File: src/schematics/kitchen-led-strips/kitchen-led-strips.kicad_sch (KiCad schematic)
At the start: 75 parts, among them Q1 BC847BS, Q2 BC847BS, U1 DML3006LFDS, U2 AP62150WU, U3 PIC16F15355-I/MV

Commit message: Started work on the PCB.
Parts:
- CONN1: renamed from CONN1a; footprint restall-generic-connectors:th-header-1x2-2.54mm-vertical -> restall-generic-connectors:th-header-1x2-5.08mm-vertical
- CONN2: renamed from CONN2a; footprint restall-generic-connectors:th-header-1x2-2.54mm-vertical -> restall-generic-connectors:th-header-1x2-5.08mm-vertical
- renumbered CONN1 to CONN-PNL1, CONN2 to CONN-PNL2, CONN2b to CONN3, CONN3 to CONN4, CONN4 to CONN5, CONN5 to CONN6, CONN6 to CONN7
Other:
- note added: "Ensure 2.5mm^{2} hole sizes for CONN1 and CONN2."
- note added: "Pin 2 of CONN2 provides flexibility in routing ground return currents."
- note added: "Pins 2 and 3 provide flexibility in routing ground return currents for the fast LED_{Dx} edges whilst avoiding potentially large DC return. Ensure 1.5mm^{2} hole sizes."
- note removed: "Pin 2 of CONN2a provides flexibility in routing ground return currents."
- note removed: "Pins 2 and 3 provide flexibility in routing ground return currents for the fast LED_{Dx} edges whilst avoiding potentially large DC return."
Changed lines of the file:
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@@
     )
   )
-  (text "Pin 2 of CONN2a provides\nflexibility in routing\nground return currents."
+  (text "Pin 2 of CONN2 provides\nflexibility in routing\nground return currents."
     (at 172.72 38.1 0)
     (effects (font (size 1.27 1.27)) (justify left bottom))
@@
     (effects (font (size 1.27 1.27)) (justify left bottom))
   )
-  (text "Pins 2 and 3 provide flexibility\nin routing ground return currents\nfor the fast LED_{Dx} edges whilst\navoiding potentially large DC return."
+  (text "Pins 2 and 3 provide flexibility\nin routing ground return currents\nfor the fast LED_{Dx} edges whilst\navoiding potentially large DC return.\n\nEnsure 1.5mm^{2} hole sizes."
     (at 212.09 69.85 0)
     (effects (font (size 1.27 1.27)) (justify left bottom))
@@
     (effects (font (size 1.27 1.27)) (justify left bottom))
   )
-  (text "Ensure 2.5mm^{2} hole sizes\nfor CONN1a and CONN2a."
-    (at 58.42 24.13 0)
+  (text "Ensure 2.5mm^{2} hole sizes\nfor CONN1 and CONN2." (at 58.42 24.13 0)
     (effects (font (size 1.27 1.27)) (justify left bottom))
   )
@@
   (symbol (lib_id "restall-generic-connectors:header-1x4") (at 38.1 242.57 0) (mirror y) (unit 1)
     (in_bom no) (on_board yes)
-    (property "Reference" "CONN6" (id 0) (at 38.1 236.22 0))
+    (property "Reference" "CONN7" (id 0) (at 38.1 236.22 0))
     (property "Value" "DNP" (id 1) (at 38.1 248.92 0)
       (effects (font (size 1.27 1.27)) hide)
@@
   (symbol (lib_id "restall-generic-connectors:header-1x2") (at 64.77 33.02 0) (unit 1)
     (in_bom no) (on_board yes)
-    (property "Reference" "CONN1a" (id 0) (at 64.77 29.21 0))
+    (property "Reference" "CONN1" (id 0) (at 64.77 29.21 0))
     (property "Value" "DNP" (id 1) (at 64.77 38.1 0)
       (effects (font (size 1.27 1.27)) hide)
     )
-    (property "Footprint" "restall-generic-connectors:th-header-1x2-2.54mm-vertical" (id 2) (at 64.77 34.29 0)
+    (property "Footprint" "restall-generic-connectors:th-header-1x2-5.08mm-vertical" (id 2) (at 64.77 34.29 0)
       (effects (font (size 1.27 1.27)) (justify left) hide)
     )
@@
   (symbol (lib_id "restall-generic-connectors:circular-4p-shield-female") (at 204.47 43.18 0) (unit 1)
     (in_bom yes) (on_board no)
-    (property "Reference" "CONN2" (id 0) (at 204.47 36.83 0))
+    (property "Reference" "CONN-PNL2" (id 0) (at 204.47 36.83 0))
     (property "Value" "PSG01593" (id 1) (at 204.47 36.9879 0)
       (effects (font (size 1.27 1.27)) hide)
@@
   (symbol (lib_id "restall-generic-connectors:header-1x5") (at 38.1 129.54 0) (mirror y) (unit 1)
     (in_bom yes) (on_board yes) (fields_autoplaced)
-    (property "Reference" "CONN3" (id 0) (at 38.1 122.0272 0))
+    (property "Reference" "CONN4" (id 0) (at 38.1 122.0272 0))
     (property "Value" "S5B-PH-K-S" (id 1) (at 38.1 137.16 0)
       (effects (font (size 1.27 1.27)) hide)
@@
   (symbol (lib_id "restall-generic-connectors:circular-4p-shield-male") (at 38.1 30.48 0) (mirror y) (unit 1)
     (in_bom yes) (on_board no)
-    (property "Reference" "CONN1" (id 0) (at 38.1 24.13 0))
+    (property "Reference" "CONN-PNL1" (id 0) (at 38.1 24.13 0))
     (property "Value" "PSG01593" (id 1) (at 38.1 24.2879 0)
       (effects (font (size 1.27 1.27)) hide)
@@
   (symbol (lib_id "restall-generic-connectors:header-1x2") (at 190.5 45.72 0) (unit 1)
     (in_bom no) (on_board yes)
-    (property "Reference" "CONN2a" (id 0) (at 190.5 41.91 0))
+    (property "Reference" "CONN2" (id 0) (at 190.5 41.91 0))
     (property "Value" "DNP" (id 1) (at 190.5 50.8 0)
       (effects (font (size 1.27 1.27)) hide)
     )
-    (property "Footprint" "restall-generic-connectors:th-header-1x2-2.54mm-vertical" (id 2) (at 190.5 46.99 0)
+    (property "Footprint" "restall-generic-connectors:th-header-1x2-5.08mm-vertical" (id 2) (at 190.5 46.99 0)
       (effects (font (size 1.27 1.27)) (justify left) hide)
     )
@@
   (symbol (lib_id "restall-generic-connectors:header-2x13-row") (at 355.6 186.69 0) (unit 1)
     (in_bom yes) (on_board yes) (fields_autoplaced)
-    (property "Reference" "CONN4" (id 0) (at 355.6 169.0172 0))
+    (property "Reference" "CONN5" (id 0) (at 355.6 169.0172 0))
     (property "Value" "header-2x13-row" (id 1) (at 355.6 204.47 0)
       (effects (font (size 1.27 1.27)) hide)
@@
   (symbol (lib_id "restall-generic-connectors:header-1x4") (at 204.47 66.04 0) (unit 1)
     (in_bom no) (on_board yes)
-    (property "Reference" "CONN2b" (id 0) (at 204.47 59.69 0))
+    (property "Reference" "CONN3" (id 0) (at 204.47 59.69 0))
     (property "Value" "DNP" (id 1) (at 204.47 72.39 0)
       (effects (font (size 1.27 1.27)) hide)
@@
   (symbol (lib_id "restall-generic-connectors:header-1x3") (at 38.1 215.9 0) (mirror y) (unit 1)
     (in_bom no) (on_board yes)
-    (property "Reference" "CONN5" (id 0) (at 38.1 210.82 0))
+    (property "Reference" "CONN6" (id 0) (at 38.1 210.82 0))
     (property "Value" "DNP" (id 1) (at 38.1 220.98 0)
       (effects (font (size 1.27 1.27)) hide)
@@
     )
     (path "/9a142532-284e-4874-93eb-221454c53190"
-      (reference "CONN1") (unit 1) (value "PSG01593") (footprint "")
-    )
-    (path "/46a48df0-1a61-4449-a89d-0b8eb64f03aa"
-      (reference "CONN1a") (unit 1) (value "DNP") (footprint "restall-generic-connectors:th-header-1x2-2.54mm-vertical")
+      (reference "CONN-PNL1") (unit 1) (value "PSG01593") (footprint "")
     )
     (path "/5a1af3aa-9b9f-4761-829a-52544f977847"
-      (reference "CONN2") (unit 1) (value "PSG01593") (footprint "")
+      (reference "CONN-PNL2") (unit 1) (value "PSG01593") (footprint "")
+    )
+    (path "/46a48df0-1a61-4449-a89d-0b8eb64f03aa"
+      (reference "CONN1") (unit 1) (value "DNP") (footprint "restall-generic-connectors:th-header-1x2-5.08mm-vertical")
     )
     (path "/ace48297-32e6-49e5-9bb8-e1575f6ce63d"
-      (reference "CONN2a") (unit 1) (value "DNP") (footprint "restall-generic-connectors:th-header-1x2-2.54mm-vertical")
+      (reference "CONN2") (unit 1) (value "DNP") (footprint "restall-generic-connectors:th-header-1x2-5.08mm-vertical")
     )
     (path "/ccd6742c-ee7b-4f1b-8b67-1ad6b59cb609"
-      (reference "CONN2b") (unit 1) (value "DNP") (footprint "restall-generic-connectors:th-header-1x4-2.54mm-vertical")
+      (reference "CONN3") (unit 1) (value "DNP") (footprint "restall-generic-connectors:th-header-1x4-2.54mm-vertical")
     )
     (path "/9584183b-267d-424a-93ae-2ff8cd487262"
-      (reference "CONN3") (unit 1) (value "S5B-PH-K-S") (footprint "restall-manufacturer-jst:S5B-PH-K-?")
+      (reference "CONN4") (unit 1) (value "S5B-PH-K-S") (footprint "restall-manufacturer-jst:S5B-PH-K-?")
     )
     (path "/b4f828f9-11d8-4383-9ef9-a3ab50143598"
-      (reference "CONN4") (unit 1) (value "header-2x13-row") (footprint "restall-generic-connectors:th-header-2x13-2.54mm-row-horizontal-shrouded")
+      (reference "CONN5") (unit 1) (value "header-2x13-row") (footprint "restall-generic-connectors:th-header-2x13-2.54mm-row-horizontal-shrouded")
     )
     (path "/fe826b18-1d9a-49b3-a833-9d426fac047e"
-      (reference "CONN5") (unit 1) (value "DNP") (footprint "restall-generic-connectors:th-header-1x3-2.54mm-vertical")
+      (reference "CONN6") (unit 1) (value "DNP") (footprint "restall-generic-connectors:th-header-1x3-2.54mm-vertical")
     )
     (path "/3ba1db20-d7d4-4ba6-aa39-1e6c8b6b2a99"
-      (reference "CONN6") (unit 1) (value "DNP") (footprint "restall-generic-connectors:th-header-1x4-2.54mm-vertical")
+      (reference "CONN7") (unit 1) (value "DNP") (footprint "restall-generic-connectors:th-header-1x4-2.54mm-vertical")
     )
     (path "/8b363bb9-6e9a-40ed-b125-c224f2d74a2d"

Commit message: Started the PCB layout.
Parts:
- CONN1, CONN2: footprint restall-generic-connectors:th-header-1x2-5.08mm-vertical -> kitchen-led-strips:th-pads-1x2-5.08mm-vertical-2.5mm^2-solder-pads
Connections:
- net MCU_ICSP_{CLK}: now also D2.3 (K); no longer D2.1 (K)
- net MCU_ICSP_{DAT}: now also D2.1 (K); no longer D2.3 (K)
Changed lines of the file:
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@@
     (pin "2")
   )
-  (symbol (lib_id "restall-manufacturer-nexperia:BZA856AVL,115") (at 76.2 132.08 270) (unit 2)
+  (symbol (lib_id "restall-manufacturer-nexperia:BZA856AVL,115") (at 76.2 132.08 270) (unit 1)
     (in_bom yes) (on_board yes) (fields_autoplaced)
     (property "Reference" "D2" (id 0) (at 78.232 130.9278 90)
@@
       (effects (font (size 1.27 1.27)) hide)
     )
-    (property "Footprint" "restall-generic-connectors:th-header-1x2-5.08mm-vertical" (id 2) (at 64.77 34.29 0)
+    (property "Footprint" "kitchen-led-strips:th-pads-1x2-5.08mm-vertical-2.5mm^2-solder-pads" (id 2) (at 64.77 34.29 0)
       (effects (font (size 1.27 1.27)) (justify left) hide)
     )
@@
     (pin "1")
   )
-  (symbol (lib_id "restall-manufacturer-nexperia:BZA856AVL,115") (at 69.85 132.08 270) (unit 1)
+  (symbol (lib_id "restall-manufacturer-nexperia:BZA856AVL,115") (at 69.85 132.08 270) (unit 2)
     (in_bom yes) (on_board yes)
     (property "Reference" "D2" (id 0) (at 63.5 120.6531 90)
@@
       (effects (font (size 1.27 1.27)) hide)
     )
-    (property "Footprint" "restall-generic-connectors:th-header-1x2-5.08mm-vertical" (id 2) (at 190.5 46.99 0)
+    (property "Footprint" "kitchen-led-strips:th-pads-1x2-5.08mm-vertical-2.5mm^2-solder-pads" (id 2) (at 190.5 46.99 0)
       (effects (font (size 1.27 1.27)) (justify left) hide)
     )
@@
     )
     (path "/46a48df0-1a61-4449-a89d-0b8eb64f03aa"
-      (reference "CONN1") (unit 1) (value "DNP") (footprint "restall-generic-connectors:th-header-1x2-5.08mm-vertical")
+      (reference "CONN1") (unit 1) (value "DNP") (footprint "kitchen-led-strips:th-pads-1x2-5.08mm-vertical-2.5mm^2-solder-pads")
     )
     (path "/ace48297-32e6-49e5-9bb8-e1575f6ce63d"
-      (reference "CONN2") (unit 1) (value "DNP") (footprint "restall-generic-connectors:th-header-1x2-5.08mm-vertical")
+      (reference "CONN2") (unit 1) (value "DNP") (footprint "kitchen-led-strips:th-pads-1x2-5.08mm-vertical-2.5mm^2-solder-pads")
     )
     (path "/ccd6742c-ee7b-4f1b-8b67-1ad6b59cb609"
@@
       (reference "D1") (unit 4) (value "BZA856AVL,115") (footprint "restall-generic-sot:SOT-353")
     )
-    (path "/8f9320d9-1ce6-4107-a4b7-9c2bd5f68690"
+    (path "/1518b9e6-2eb2-4972-9aed-ba756bbb64fb"
       (reference "D2") (unit 1) (value "BZA856AVL,115") (footprint "restall-generic-sot:SOT-353")
     )
-    (path "/1518b9e6-2eb2-4972-9aed-ba756bbb64fb"
+    (path "/8f9320d9-1ce6-4107-a4b7-9c2bd5f68690"
       (reference "D2") (unit 2) (value "BZA856AVL,115") (footprint "restall-generic-sot:SOT-353")
     )

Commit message: Further elaboration of the PCB.
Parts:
- renumbered D5 to D4, D6 to D5, D4 to D6
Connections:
- net +5Vdc: now also CONN5.21 (P21), CONN5.26 (P26), D1.1 (K), D1.3 (K); no longer CONN5.17 (P17), CONN5.2 (P2), D1.4 (K), D1.5 (K)
- net GND: now also CONN5.2 (P2); no longer CONN5.26 (P26)
- net GPIO_{0}: now also CONN5.19 (P19); no longer CONN5.25 (P25)
- net GPIO_{1}: now also CONN5.17 (P17); no longer CONN5.23 (P23)
- net GPIO_{2}: now also CONN5.15 (P15), D4.5 (K); no longer CONN5.21 (P21), D4.4 (K)
- net GPIO_{3}: now also CONN5.13 (P13), D4.4 (K); no longer CONN5.19 (P19), D4.5 (K)
- net GPOC_{0}: now also CONN5.9 (P9), D6.5 (K), Q1.3 (C); no longer CONN5.15 (P15), D5.3 (K), Q1.6 (C)
- net GPOC_{1}: now also CONN5.7 (P7), D6.1 (K), Q1.6 (C); no longer CONN5.13 (P13), D5.1 (K), Q1.3 (C)
- net IR_LED: now also CONN5.23 (P23), D5.1 (K); no longer CONN5.3 (P3), D6.1 (K)
- net IR_REC: now also CONN5.25 (P25), D5.3 (K); no longer CONN5.1 (P1), D6.3 (K)
- net I^{2}C_SCL: now also CONN5.3 (P3), D6.3 (K); no longer CONN5.9 (P9), D6.4 (K)
- net I^{2}C_SDA: now also CONN5.1 (P1), D6.4 (K); no longer CONN5.7 (P7), D6.5 (K)
- net LED_{D0}: now also D1.5 (K); no longer D1.3 (K)
- net LED_{D1}: now also D1.4 (K); no longer D1.1 (K)
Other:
- note added: "TODO: ADD 5mil TRACE Z TO LIST ABOVE..."
- moved on the sheet: C13, D3, D4A, D4B, D4C, D4D, D5A, D5B, D5C, D5D, D6A, D6B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

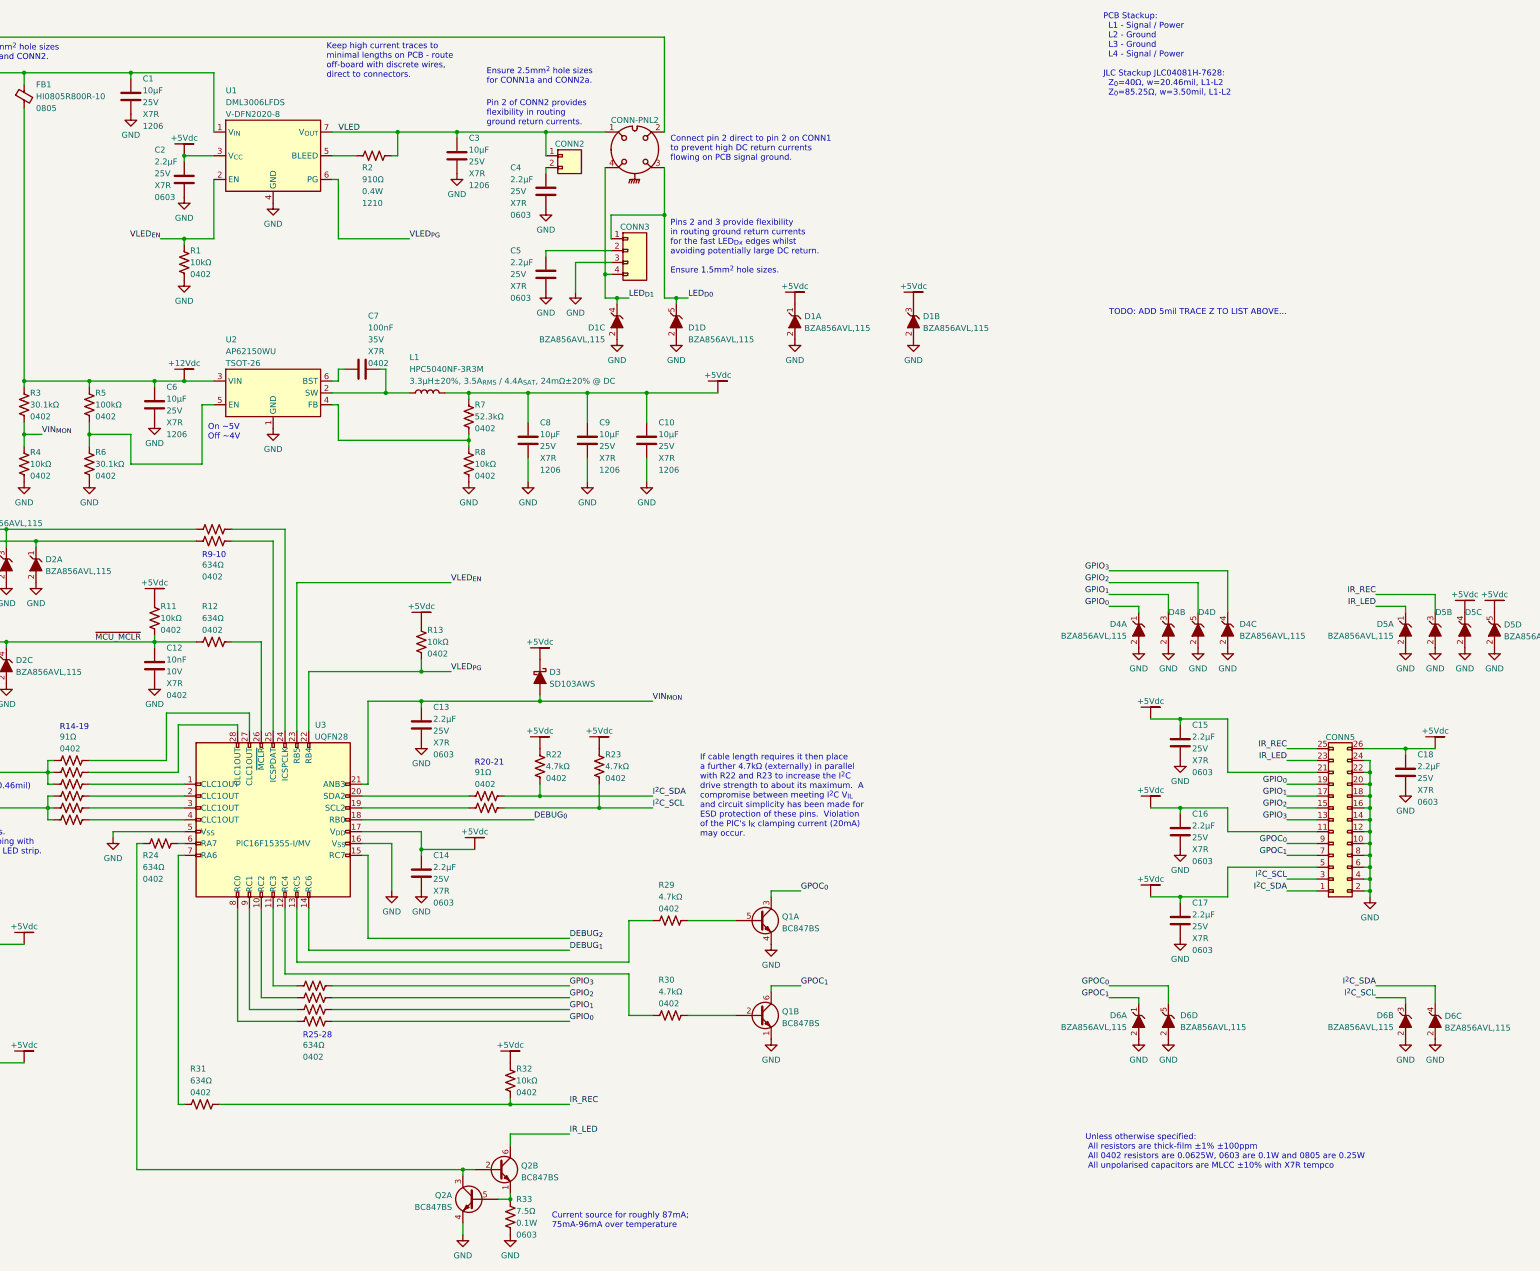
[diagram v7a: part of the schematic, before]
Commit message: Further PCB elaboration.  Almost ready for fabrication.
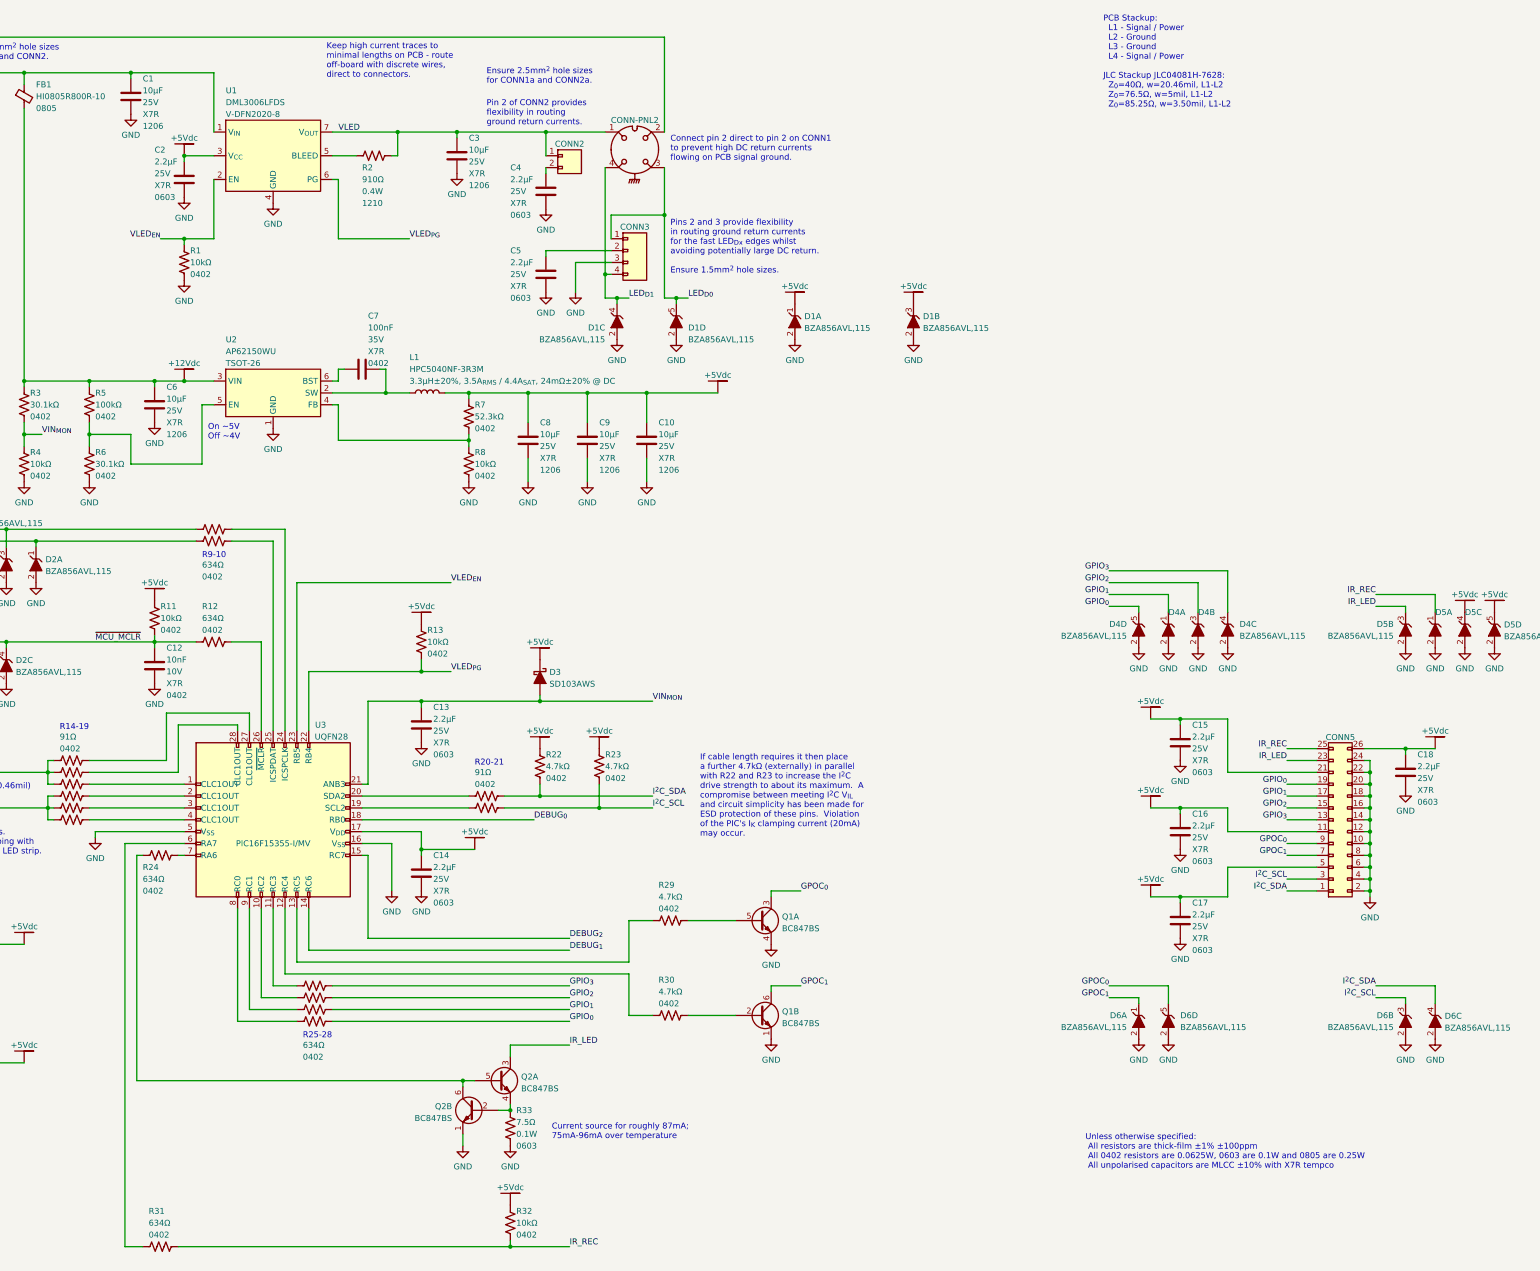
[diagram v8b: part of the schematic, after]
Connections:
- net GND: now also Q2.1 (E); no longer Q2.4 (E)
- net GPIO_{0}: now also D4.5 (K); no longer D4.1 (K)
- net GPIO_{1}: now also D4.1 (K); no longer D4.3 (K)
- net GPIO_{2}: now also D4.3 (K); no longer D4.5 (K)
- net IR_LED: now also D5.3 (K), Q2.3 (C); no longer D5.1 (K), Q2.6 (C)
- net IR_REC: now also D5.1 (K); no longer D5.3 (K)
- net at R24.2: now also U3.7 (RA6); no longer U3.6 (RA7)
- net at R31.1: now also U3.6 (RA7); no longer U3.7 (RA6)
- new net: Q2.2 (B), Q2.4 (E), R33.1
- new net: Q2.5 (B), Q2.6 (C), R24.1
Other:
- note added: "PCB Stackup: L1 - Signal / Power L2 - Ground L3 - Ground L4 - Signal / Power JLC Stackup JLC04081H-7628: Z_{0}=40Ω, w=20.46mil, L1-L2 Z_{0}=76.5Ω, w=5mil, L1-L2 Z_{0}=85.25Ω, w=3.50mil, L1-L2"
- note removed: "PCB Stackup: L1 - Signal / Power L2 - Ground L3 - Ground L4 - Signal / Power JLC Stackup JLC04081H-7628: Z_{0}=40Ω, w=20.46mil, L1-L2 Z_{0}=85.25Ω, w=3.50mil, L1-L2"
- note removed: "TODO: ADD 5mil TRACE Z TO LIST ABOVE..."
- moved on the sheet: Q2A, Q2B, R24, R31, R32, R33
